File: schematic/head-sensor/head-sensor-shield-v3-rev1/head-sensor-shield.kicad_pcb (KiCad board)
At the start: 2 copper layers, 61.5 x 34.8 mm, 39 parts, among them K1 Power, P1 USB, P2 Zone2, P3 MCU1, P4 USART1, P5 EXTENSION-CONNECTOR, P6 MCU2, P8 NRF24L01, P9 Zone1, Q1 MOSFET_P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

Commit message: Some job for registering unknown commads
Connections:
- U2 pad 2: (no net) -> GND
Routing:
- net GND: track 35.9 -> 39.6 mm, vias 6 -> 7

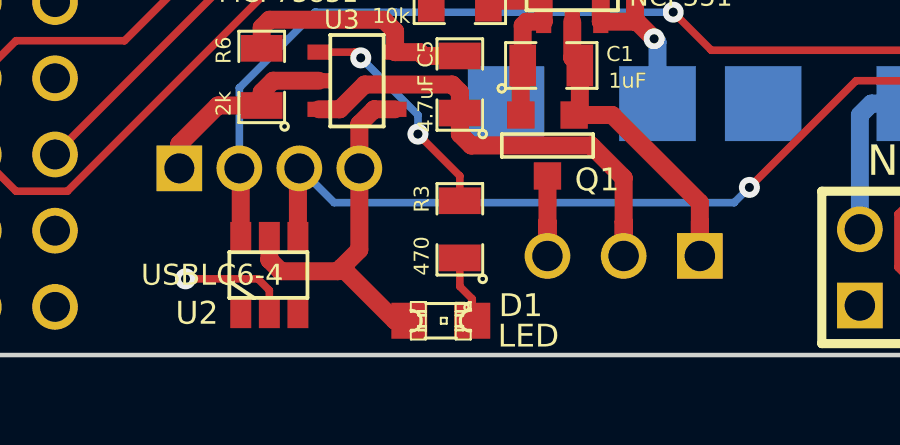
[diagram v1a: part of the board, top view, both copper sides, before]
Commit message: New sensor module for LW round plastic sensor; leds are 1206, capacitors fixed
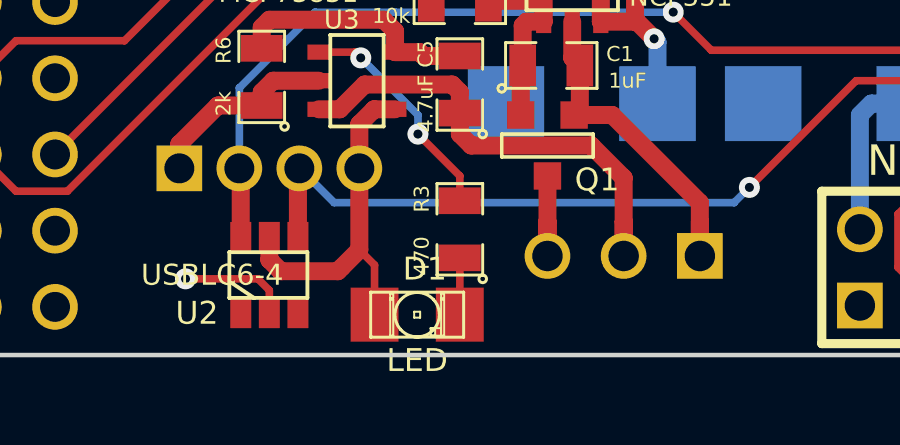
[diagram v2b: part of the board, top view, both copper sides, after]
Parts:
- D1: footprint LED-0805 -> LED-1206
- moved D1 0.81 mm to (78.8, 70.8)
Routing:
- net N-0000036: track 12.8 -> 12.2 mm
